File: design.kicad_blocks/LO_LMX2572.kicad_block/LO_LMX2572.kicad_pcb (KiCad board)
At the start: 2 copper layers, 56 parts

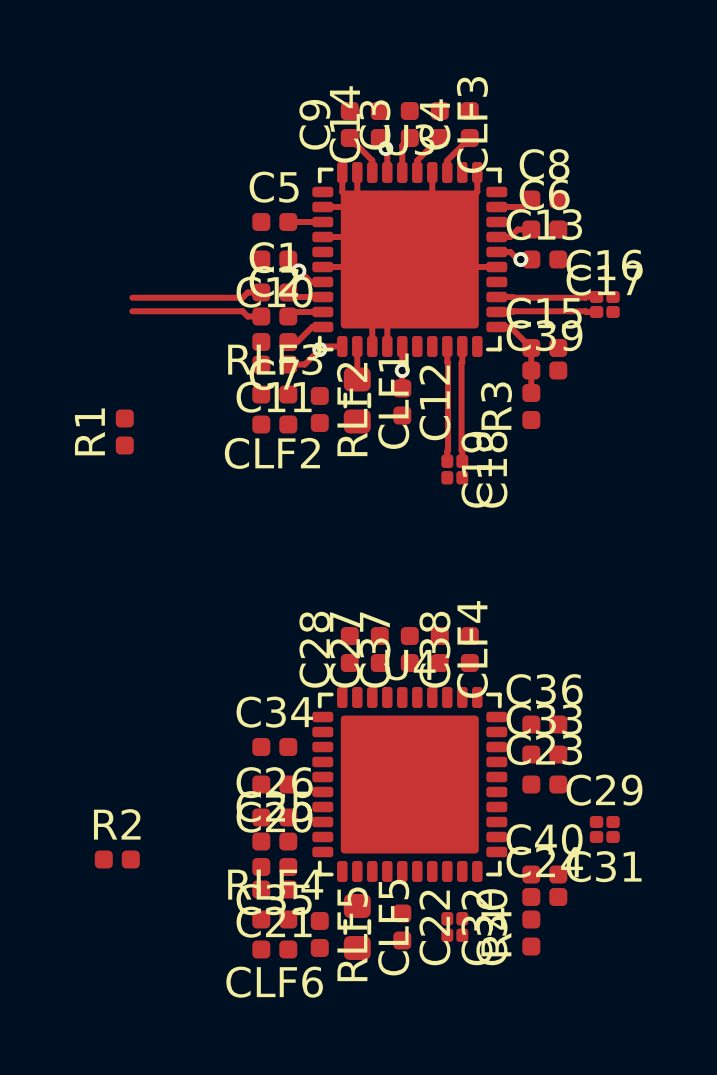
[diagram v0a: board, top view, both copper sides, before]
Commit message: used instanced sheet for LO, design block, synth placement
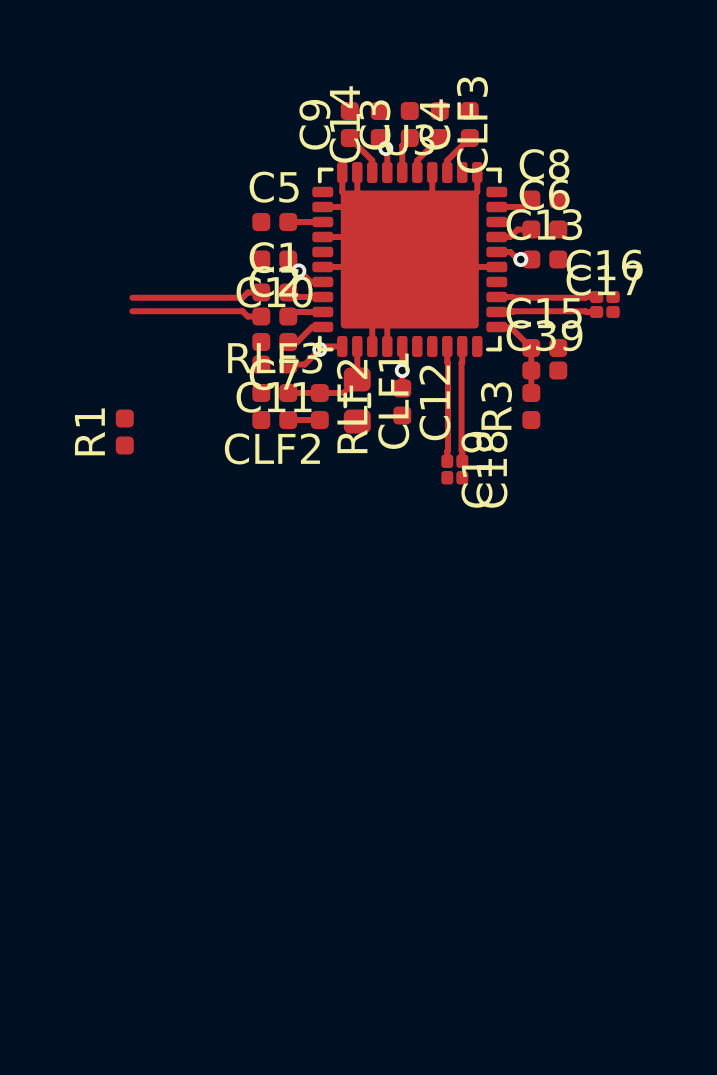
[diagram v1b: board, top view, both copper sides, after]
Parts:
- removed C20, C21, C24, C25, C26, C33: 100nF, ar_passives:C_0402
- removed C22, C23, C27, C35, C40: 1uF, ar_passives:C_0402
- removed C28: 10nF, ar_passives:C_0402
- removed C29, C30, C31, C32: 22pF, ar_passives:C_0201
- removed C34: 470nF, ar_passives:C_0402
- removed C36, C37, C38: 10uF, ar_passives:C_0402
- removed CLF4, CLF6: 0pF, ar_passives:C_0402
- removed CLF5: 0pF, ar_passives:C_0603
- removed R2, R4: 0R, ar_passives:R_0402
- removed RLF4, RLF5: TBD, ar_passives:R_0402
- removed U4: ~, ar_ic:QFN40
- moved CLF2 0.15 mm to (102.5, 77.8)
- moved RLF2 0.10 mm to (104.0, 77.4)
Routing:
- net /LO1/CPOut: track 1.10 -> 3.59 mm
- net Net-(CLF2-Pad1): track 0.14 -> 1.19 mm
